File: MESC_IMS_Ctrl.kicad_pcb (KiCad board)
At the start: 4 copper layers, 120 x 75 mm, 172 parts, among them J1 Conn_01x08_Female, J2 Conn_01x08_Female, J3 Conn_01x08_Female, J4 Conn_01x06_Male, J5 Conn_ARM_JTAG_SWD_10, J6 USB_C_Receptacle_USB2.0, J7 Conn_01x03_Male, J8 Conn_01x04_Male, J9 Conn_01x08_Male, U1 STM32F303CBTx, U2 LM5017MR, U3 TPS76333, U4 INA240A1PW, U5 UCC21520DW, U6 INA240A1PW, U7 UCC21520DW, U8 INA240A1PW, U9 UCC21520DW, Y1 ASE-8.000MHZ-LC-T

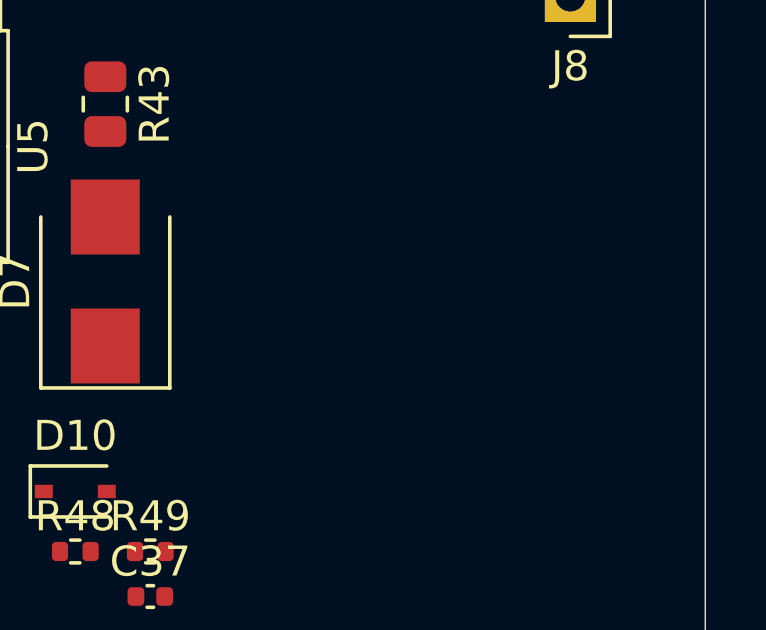
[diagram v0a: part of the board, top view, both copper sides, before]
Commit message: Adding low-side current comparators
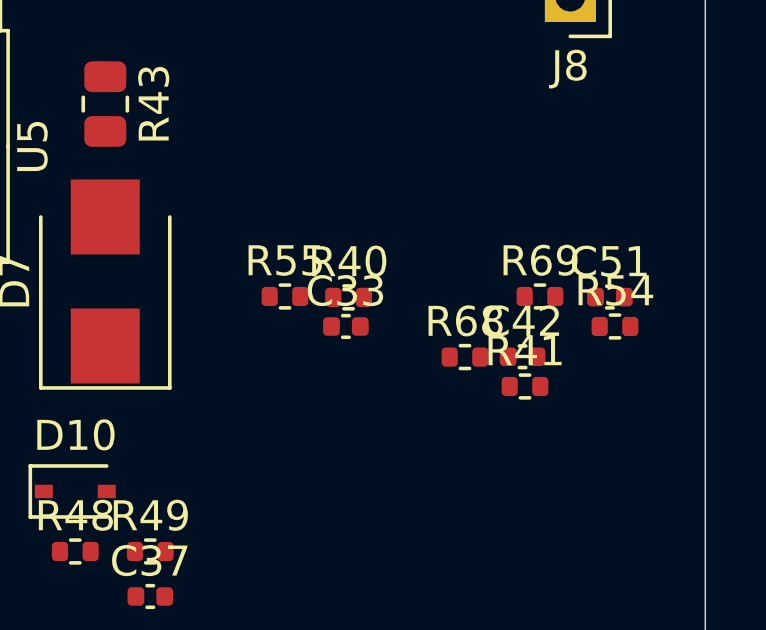
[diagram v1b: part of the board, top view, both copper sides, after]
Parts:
- added C33: 100pF 16V, Capacitor_SMD:C_0402_1005Metric, F.Cu at (208.0, 115.0)
- added C42: 100pF 16V, Capacitor_SMD:C_0402_1005Metric, F.Cu at (213.9, 116.0)
- added C51: 100pF 16V, Capacitor_SMD:C_0402_1005Metric, F.Cu at (216.8, 114.0)
- added R40: 150R, Resistor_SMD:R_0402_1005Metric, F.Cu at (208.1, 114.0)
- added R41: 150R, Resistor_SMD:R_0402_1005Metric, F.Cu at (214.0, 117.0)
- added R54: 150R, Resistor_SMD:R_0402_1005Metric, F.Cu at (217.0, 115.0)
- added R55: 4k7, Resistor_SMD:R_0402_1005Metric, F.Cu at (206.0, 114.0)
- added R68: 4k7, Resistor_SMD:R_0402_1005Metric, F.Cu at (212.0, 116.0)
- added R69: 4k7, Resistor_SMD:R_0402_1005Metric, F.Cu at (214.5, 114.0)
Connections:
- net /Phase_U/curr_sen+ renamed /ISU
- net /Phase_V/curr_sen+ renamed /ISV
- net /Phase_W/curr_sen+ renamed /ISW

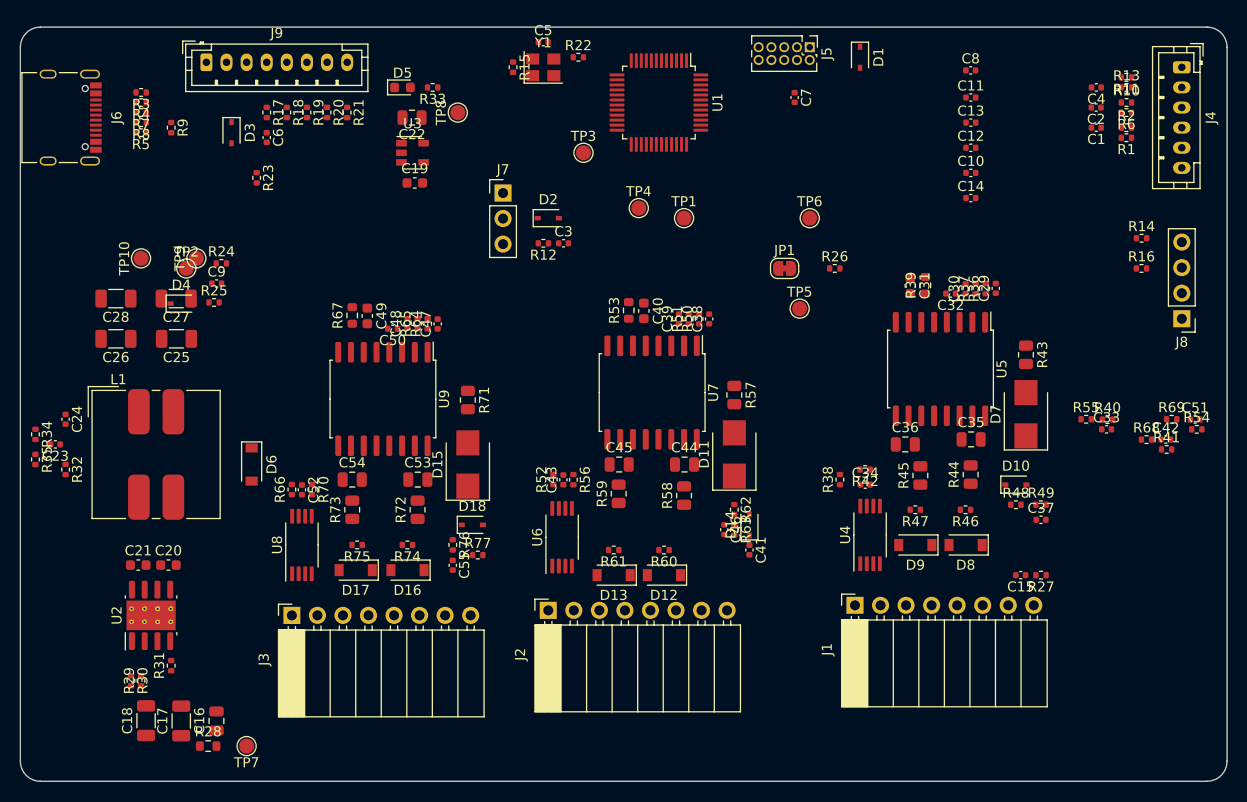
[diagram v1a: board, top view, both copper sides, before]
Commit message: Adding LCSC part numbers
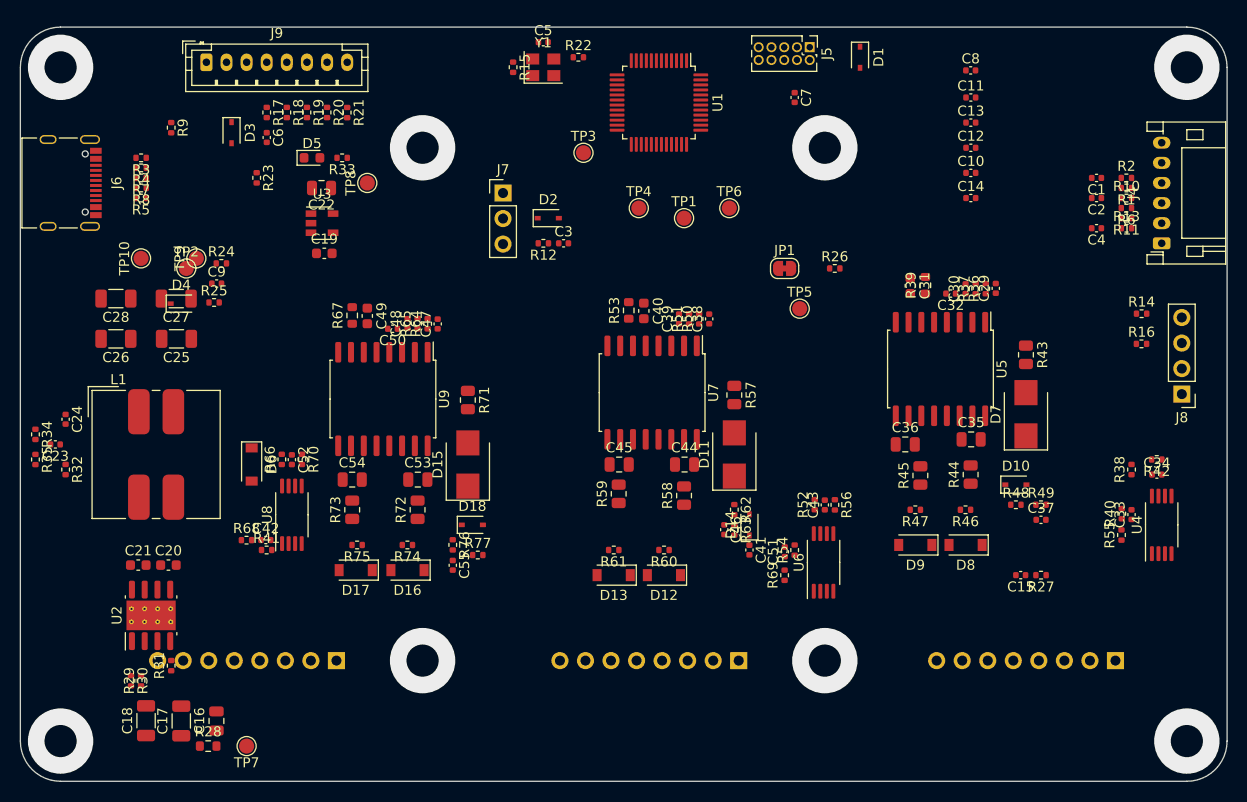
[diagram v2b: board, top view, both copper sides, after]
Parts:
- J1, J2, J3: footprint Connector_PinSocket_2.54mm:PinSocket_1x08_P2.54mm_Horizontal -> Connector_PinSocket_2.54mm:PinSocket_1x08_P2.54mm_Vertical; moved to B.Cu
- J4: footprint Connector_JST:JST_PH_B6B-PH-K_1x06_P2.00mm_Vertical -> Connector_JST:JST_PH_S6B-PH-K_1x06_P2.00mm_Horizontal
- moved R41 90.1 mm to (124.5, 127.0)
- moved R68 90.1 mm to (122.5, 126.0)
- moved C42 90.1 mm to (124.4, 126.0)
- moved C51 42.9 mm to (176.0, 127.2), turned to 90 degrees
- moved R54 41.8 mm to (177.0, 127.0), turned to 90 degrees
- moved R69 41.5 mm to (176.0, 129.5), turned to 90 degrees
- moved C34 29.0 mm to (213.0, 119.5)
- moved R38 29.0 mm to (210.5, 119.0)
- moved R42 29.0 mm to (213.0, 118.0)
- moved U4 29.0 mm to (213.5, 124.5)
- moved J1 26.5 mm to (208.9, 138.0)
- moved C43 26.1 mm to (180.0, 122.5)
- moved R52 26.1 mm to (179.0, 122.5)
- moved R56 26.1 mm to (181.0, 122.5)
- moved U6 26.1 mm to (179.9, 128.2)
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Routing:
- net (no net): vias 0 -> 8
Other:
- outline, holes or cut-outs redrawn

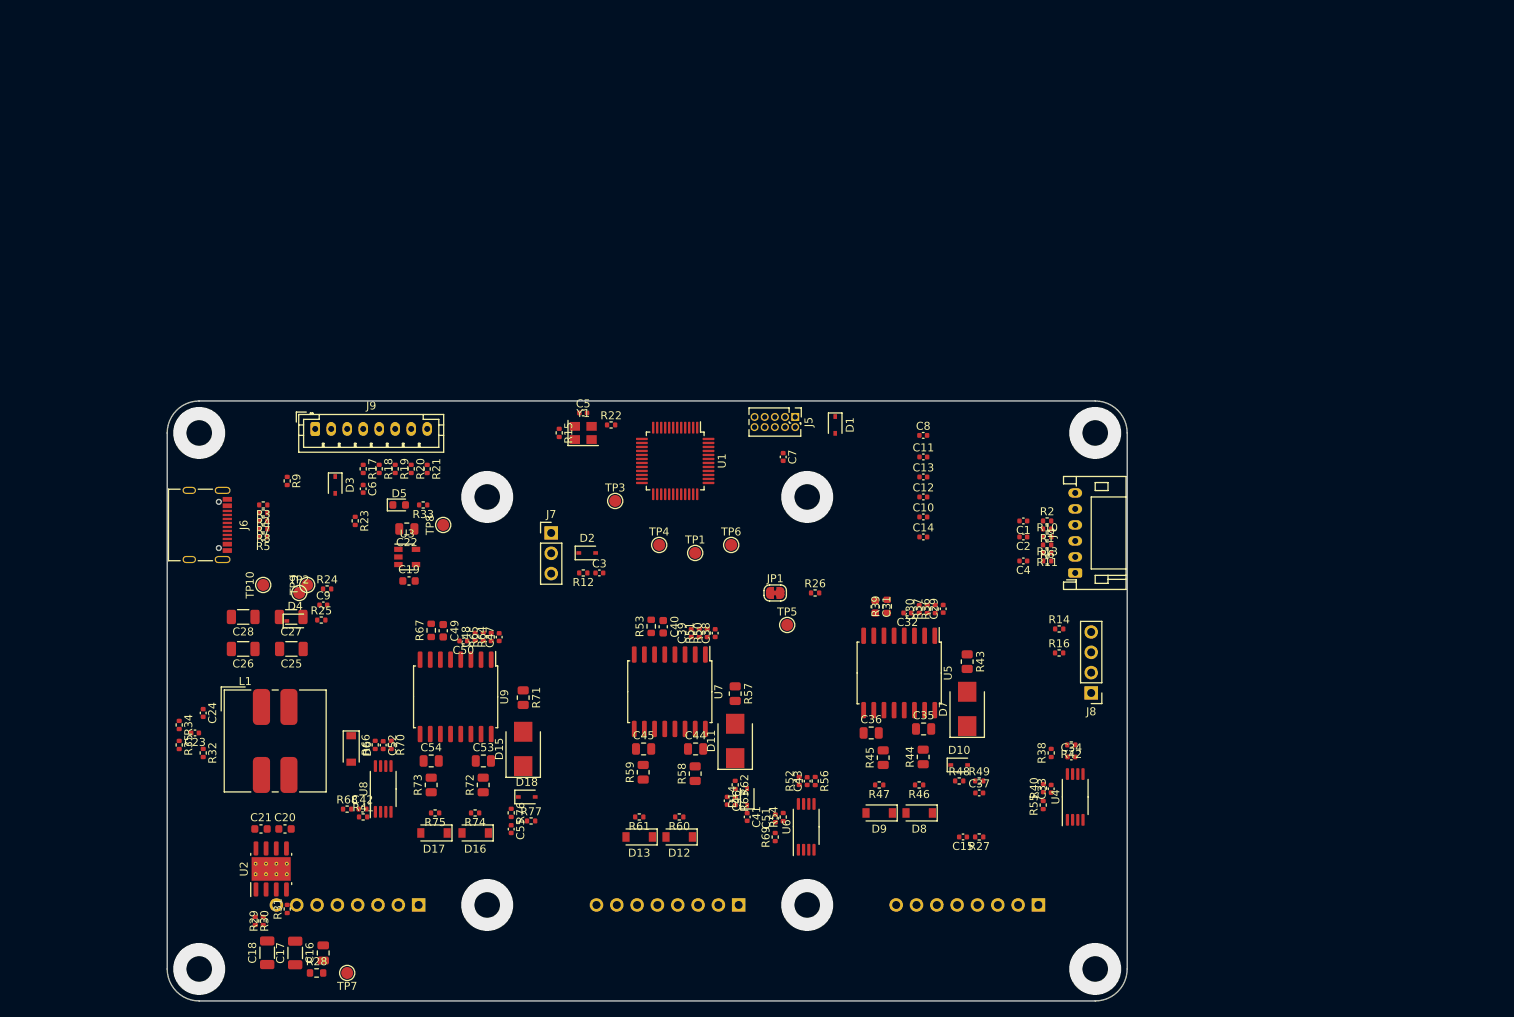
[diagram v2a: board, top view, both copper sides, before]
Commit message: Twaeking the layout to fit into 100x100mm
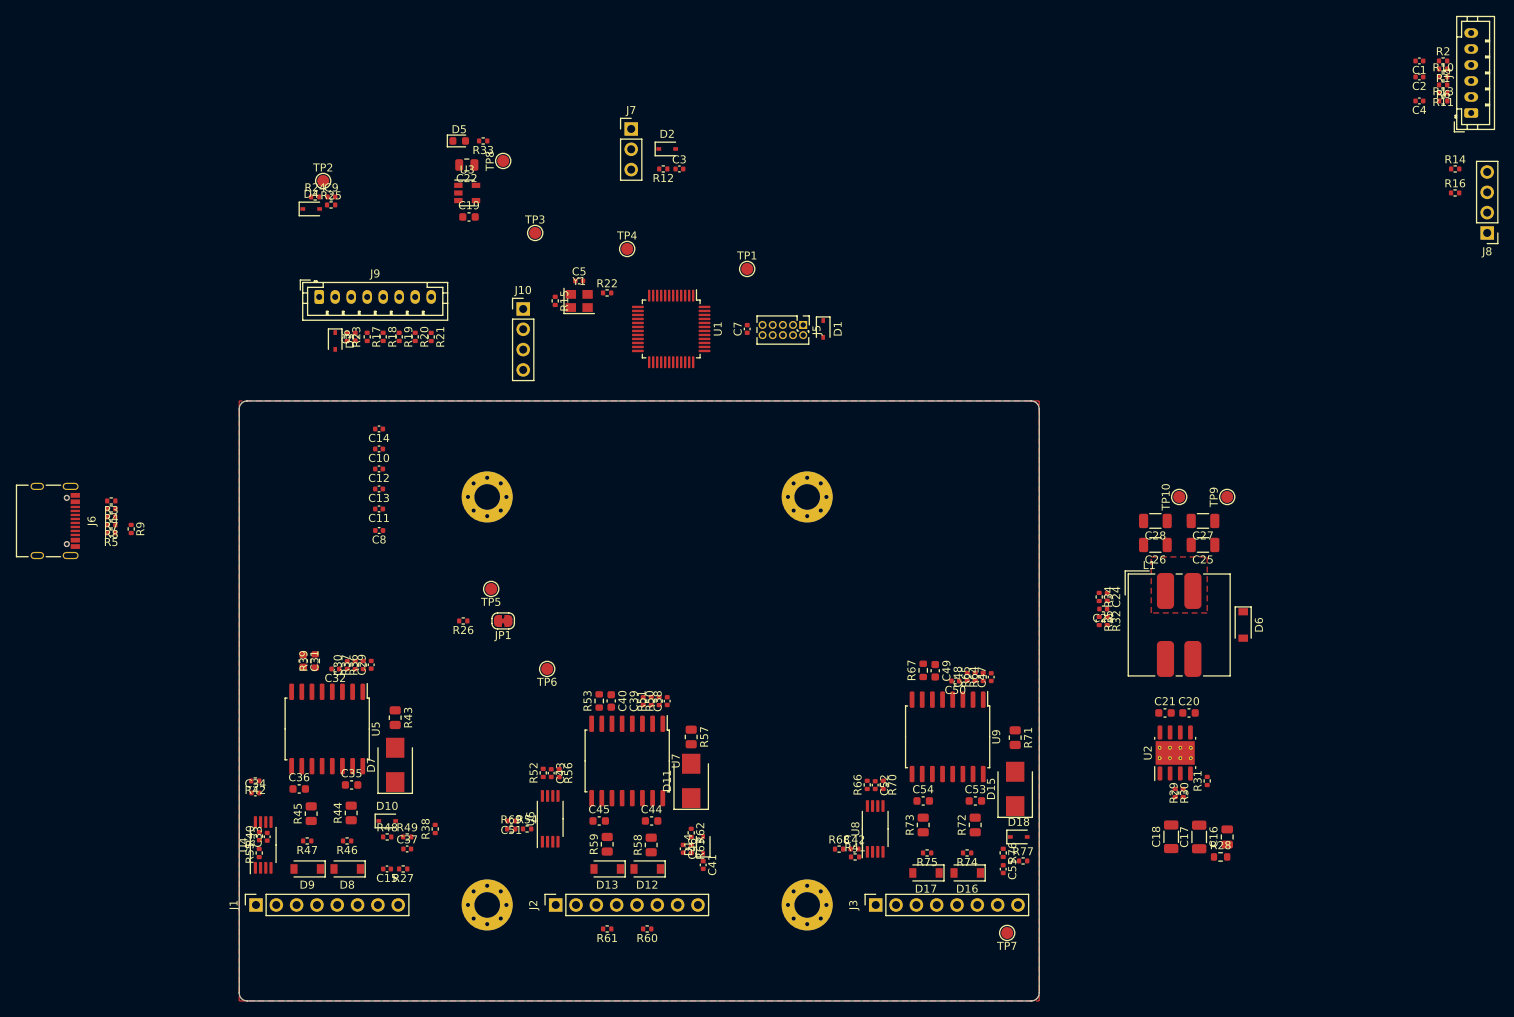
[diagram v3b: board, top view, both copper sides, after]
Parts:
- added H1: MountingHole, MountingHole:MountingHole_3.2mm_M3_Pad_Via, B.Cu at (180.0, 87.0)
- added H2: MountingHole, MountingHole:MountingHole_3.2mm_M3_Pad_Via, B.Cu at (180.0, 138.0)
- added H3: MountingHole, MountingHole:MountingHole_3.2mm_M3_Pad_Via, B.Cu at (140.0, 138.0)
- added H4: MountingHole, MountingHole:MountingHole_3.2mm_M3_Pad_Via, B.Cu at (140.0, 87.0)
- added J10: Conn_01x04_Male, Connector_PinHeader_2.54mm:PinHeader_1x04_P2.54mm_Vertical, F.Cu at (144.5, 63.5)
- added svg2mod: G***, label, B.Cu at (158.0, 108.5)
- C35, C36, C44, C45, C53, C54: footprint Capacitor_SMD:C_0805_2012Metric -> Capacitor_SMD:C_0603_1608Metric
- J1, J2, J3: moved to F.Cu
- J4: footprint Connector_JST:JST_PH_S6B-PH-K_1x06_P2.00mm_Horizontal -> Connector_JST:JST_PH_B6B-PH-K_1x06_P2.00mm_Vertical
- moved R29 116.1 mm to (227.0, 124.0)
- moved R30 116.1 mm to (226.0, 124.0)
- moved R31 116.1 mm to (230.0, 122.5)
- moved R34 116.1 mm to (216.5, 99.5)
- moved R35 116.0 mm to (216.5, 102.5)
- moved TP9 115.5 mm to (232.5, 87.0)
- moved TP10 115.0 mm to (226.5, 87.0)
- moved C26 114.8 mm to (223.5, 93.0)
- moved C25 114.7 mm to (229.5, 93.0)
- moved C28 114.7 mm to (223.5, 90.0)
- moved C27 114.6 mm to (229.5, 90.0)
- moved C23 114.6 mm to (217.0, 101.0)
- moved R32 114.2 mm to (217.5, 102.5)
- moved R28 113.9 mm to (231.7, 132.0)
- moved C16 113.9 mm to (232.5, 129.5)
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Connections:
- TP1 pad 1: /ISW_MCU -> /~RESET
- TP3 pad 1: /ISU_MCU -> /ANA_IN
- TP4 pad 1: /ISV_MCU -> /PWM_IN
- U1 pad 39: /SWO -> /PWM_IN
- U1 pad 40: /PWM_IN -> /HALL_1
- U1 pad 41: Net-(U1-Pad41) -> /HALL_2
- U1 pad 42: /HALL_1 -> /HALL_3
- U1 pad 43: /HALL_2 -> /I2C_SDA
- U1 pad 45: /HALL_3 -> /CAN_RX
- U1 pad 46: /I2C_SDA -> /CAN_TX
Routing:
- net (no net): vias 8 -> 0
- added copper zone on F.Cu, net +5V
- added copper zone on F.Cu, net GND
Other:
- board size 120 x 75 mm -> 100 x 75 mm

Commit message: More placement
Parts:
- J4: footprint Connector_JST:JST_PH_B6B-PH-K_1x06_P2.00mm_Vertical -> Connector_JST:JST_PH_S6B-PH-SM4-TB_1x06-1MP_P2.00mm_Horizontal
- J9: footprint Connector_JST:JST_PH_B8B-PH-K_1x08_P2.00mm_Vertical -> Connector_JST:JST_PH_B8B-PH-SM4-TB_1x08-1MP_P2.00mm_Vertical
- moved C9 128.2 mm to (205.5, 145.5)
- moved R25 128.2 mm to (205.5, 146.5)
- moved D4 128.2 mm to (203.0, 147.0)
- moved R24 128.2 mm to (203.5, 145.5)
- moved TP2 128.2 mm to (204.5, 143.5)
- moved R1 85.7 mm to (195.5, 90.5)
- moved R10 85.7 mm to (195.5, 91.5)
- moved R11 85.7 mm to (195.5, 93.5)
- moved R13 85.7 mm to (195.5, 94.5)
- moved R2 85.7 mm to (195.5, 89.5)
- moved R6 85.7 mm to (195.5, 92.5)
- moved C1 85.7 mm to (192.5, 89.5)
- moved C2 85.7 mm to (192.5, 91.5)
- moved C4 85.7 mm to (192.5, 94.5)
- moved R14 82.3 mm to (187.5, 83.0), turned to 90 degrees
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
